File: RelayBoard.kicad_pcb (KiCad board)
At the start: 4 copper layers, 211.1 x 95.2 mm, 118 parts, among them J1 OSTTC020162, J10 24VAC In, J11 OSTTC020162, J12 OSTTC020162, J13 OSTTC020162, J14 OSTTC020162, J15 OSTTC020162, J16 OSTTC020162, J17 OSTTC020162, J18 OSTTC020162, J19 Raspberry_Pi_2_3, J2 OSTTC020162, J20 OSTTC020162, J22 Conn_01x04, J3 OSTTC020162, J4 OSTTC020162, J5 OSTTC020162, J6 OSTTC020162, J7 OSTTC020162, J8 OSTTC020162, J9 PJ-202A, K1 AQY212GHAX, K11 AQY212GHAX, K12 AQY212GHAX, K13 AQY212GHAX, K14 AQY212GHAX, K15 AQY212GHAX, K16 AQY212GHAX, K17 AQY212GHAX, K18 AQY212GHAX, K2 AQY212GHAX, K3 AQY212GHAX, K4 AQY212GHAX, K5 AQY212GHAX, K6 AQY212GHAX, K7 AQY212GHAX, K8 AQY212GHAX, U1 AP1117-50

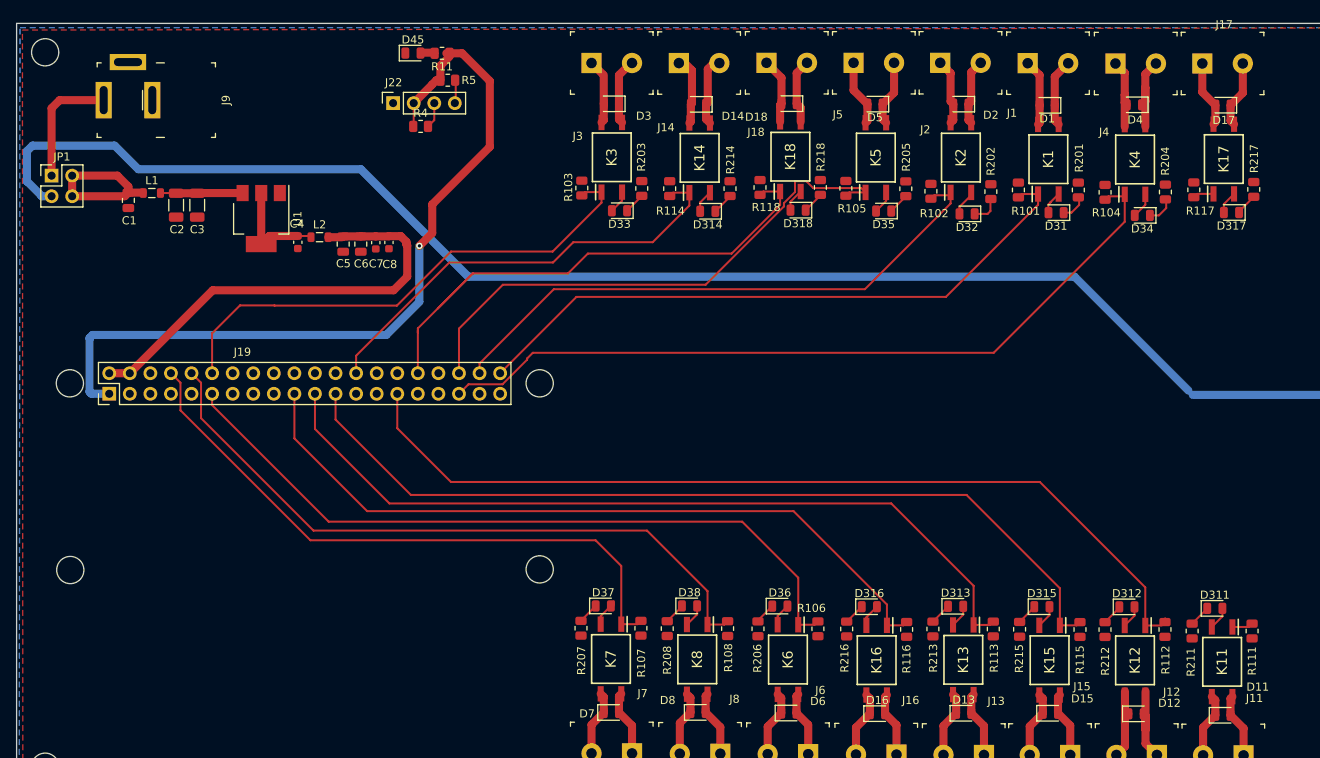
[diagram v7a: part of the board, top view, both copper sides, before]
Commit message: total rewrite, solid state relays & change all footprints to 0805s
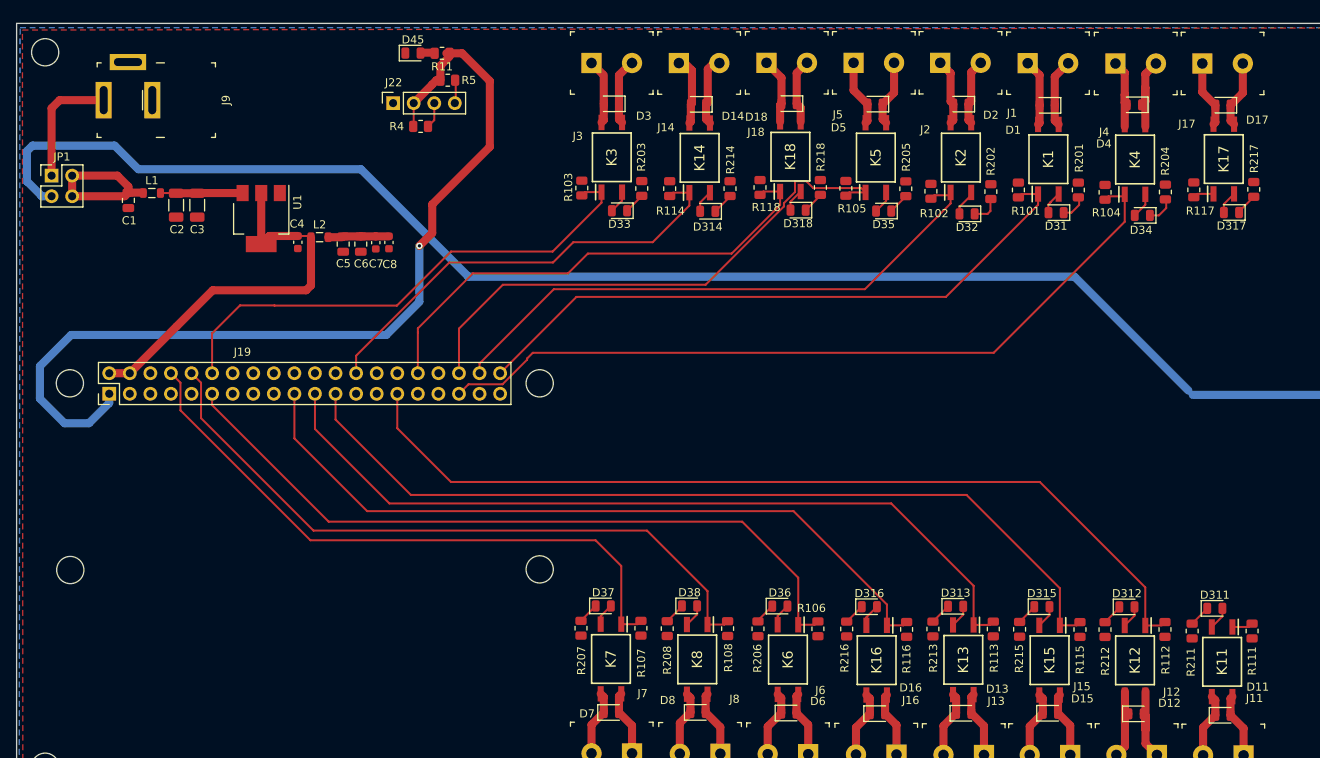
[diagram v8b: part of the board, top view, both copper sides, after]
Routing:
- net Net-(C5-Pad1): track 56.1 -> 7.59 mm
- net 5V: track 12.9 -> 48.3 mm
- net +3V3: track 100.0 -> 114.4 mm
- net Net-(J19-Pad32): track 67.3 -> 60.9 mm
- net Net-(J19-Pad29): track 112.1 -> 111.5 mm
- net Net-(D37-Pad2): track 3.29 -> 2.77 mm
